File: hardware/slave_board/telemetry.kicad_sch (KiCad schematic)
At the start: 0 parts

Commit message: feat(hw): complete Telemetry schematic, ADS1115 integration and voltage divider
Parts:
- added U2: ADS1115IDGS, Package_SO:TSSOP-10_3x3mm_P0.5mm, symbol Analog_ADC:ADS1115IDGS
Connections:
- new net +3.3V: U2.8 (VDD)
- new net ADC_ALERT: U2.2 (ALERT/RDY)
- new net GND: U2.1 (ADDR), U2.3 (GND)
- new net I2C_SCL: U2.10 (SCL)
- new net I2C_SDA: U2.9 (SDA)

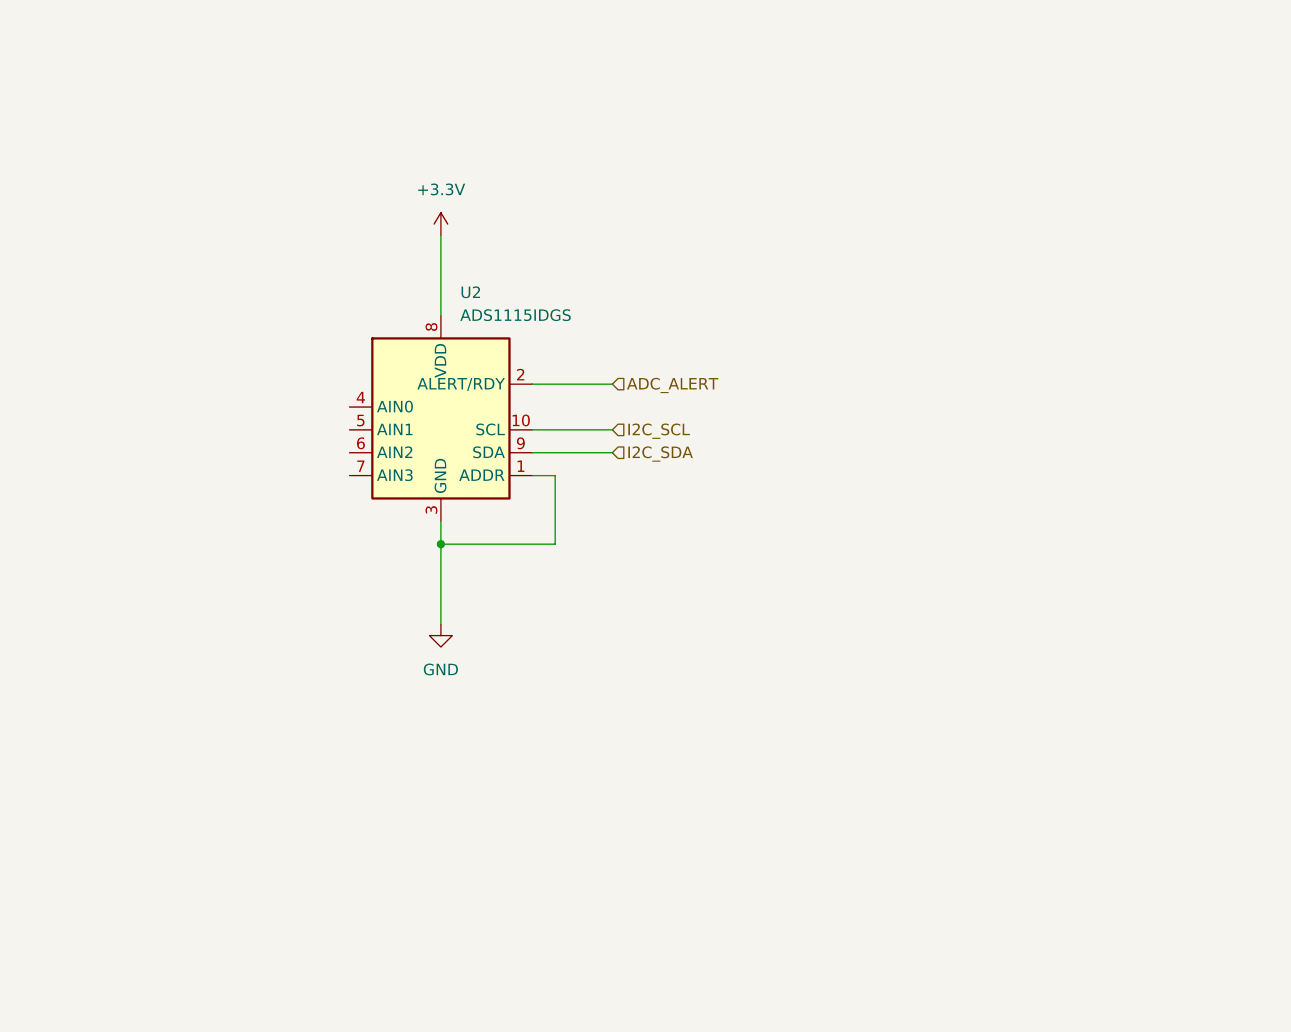
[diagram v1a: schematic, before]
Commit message: feat(hw): add Master-board RJ45 protection circuit with PTC and BAT54S clamps
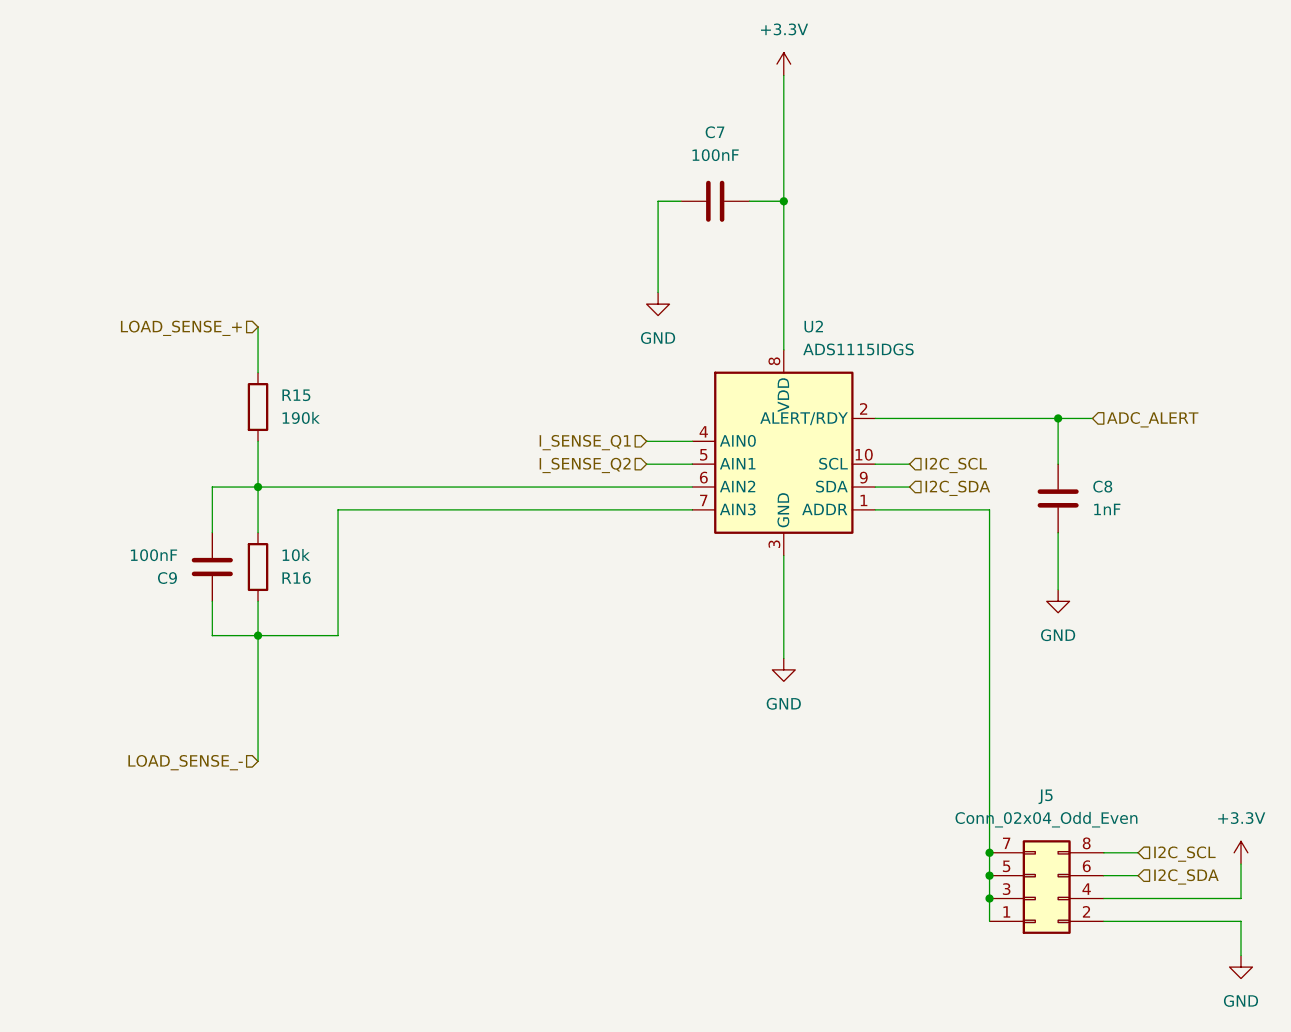
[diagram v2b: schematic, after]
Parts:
- added C7: 100nF, symbol Device:C
- added C8: 1nF, symbol Device:C
- added C9: 100nF, Capacitor_SMD:C_0805_2012Metric_Pad1.18x1.45mm_HandSolder, symbol Device:C
- added J5: Conn_02x04_Odd_Even, symbol Connector_Generic:Conn_02x04_Odd_Even
- added R15: 190k, Resistor_SMD:R_1206_3216Metric_Pad1.30x1.75mm_HandSolder, symbol Device:R
- added R16: 10k, Resistor_SMD:R_0805_2012Metric_Pad1.20x1.40mm_HandSolder, symbol Device:R
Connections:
- net +3.3V: now also C7.2, J5.4 (Pin_4)
- net ADC_ALERT: now also C8.1
- net GND: now also C7.1, C8.2, J5.2 (Pin_2); no longer U2.1 (ADDR)
- net I2C_SCL: now also J5.8 (Pin_8)
- net I2C_SDA: now also J5.6 (Pin_6)
- net I_SENSE_Q1: now reaches U2.4 (AIN0)
- net I_SENSE_Q2: now reaches U2.5 (AIN1)
- net at U2.6 (AIN2): now also C9.2, R15.2, R16.2
- net LOAD_SENSE_-: now reaches U2.7 (AIN3)
- net LOAD_SENSE_-: now also C9.1, R16.1
- new net: J5.1 (Pin_1), J5.3 (Pin_3), J5.5 (Pin_5), J5.7 (Pin_7), U2.1 (ADDR)
- new net LOAD_SENSE_+: R15.1
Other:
- moved on the sheet: U2

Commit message: hw(slave): fix footprints, enforce HandSolder, defer connector selection
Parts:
- C7, C8: footprint (none) -> Capacitor_SMD:C_0805_2012Metric_Pad1.18x1.45mm_HandSolder
- J5: footprint (none) -> Connector_PinHeader_2.54mm:PinHeader_2x04_P2.54mm_Vertical
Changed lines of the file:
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@@
 			)
 		)
-		(property "Footprint" ""
+		(property "Footprint" "Capacitor_SMD:C_0805_2012Metric_Pad1.18x1.45mm_HandSolder"
 			(at 182.5752 99.06 0)
 			(hide yes)
@@
 			)
 		)
-		(property "Description" "Unpolarized capacitor"
+		(property "Description" "Ceramic Capacitor SMD 1nF, 50V, C0G/NP0, 0805"
 			(at 181.61 95.25 0)
 			(hide yes)
@@
 			)
 		)
-		(property "Footprint" ""
+		(property "Footprint" "Capacitor_SMD:C_0805_2012Metric_Pad1.18x1.45mm_HandSolder"
 			(at 147.32 61.2648 0)
 			(hide yes)
@@
 			)
 		)
-		(property "Description" "Unpolarized capacitor"
+		(property "Description" "Ceramic Capacitor SMD 100nF, 50V, X7R, 0805"
 			(at 143.51 62.23 0)
 			(hide yes)
@@
 			)
 		)
-		(property "Footprint" ""
+		(property "Footprint" "Connector_PinHeader_2.54mm:PinHeader_2x04_P2.54mm_Vertical"
 			(at 179.07 139.7 0)
 			(hide yes)

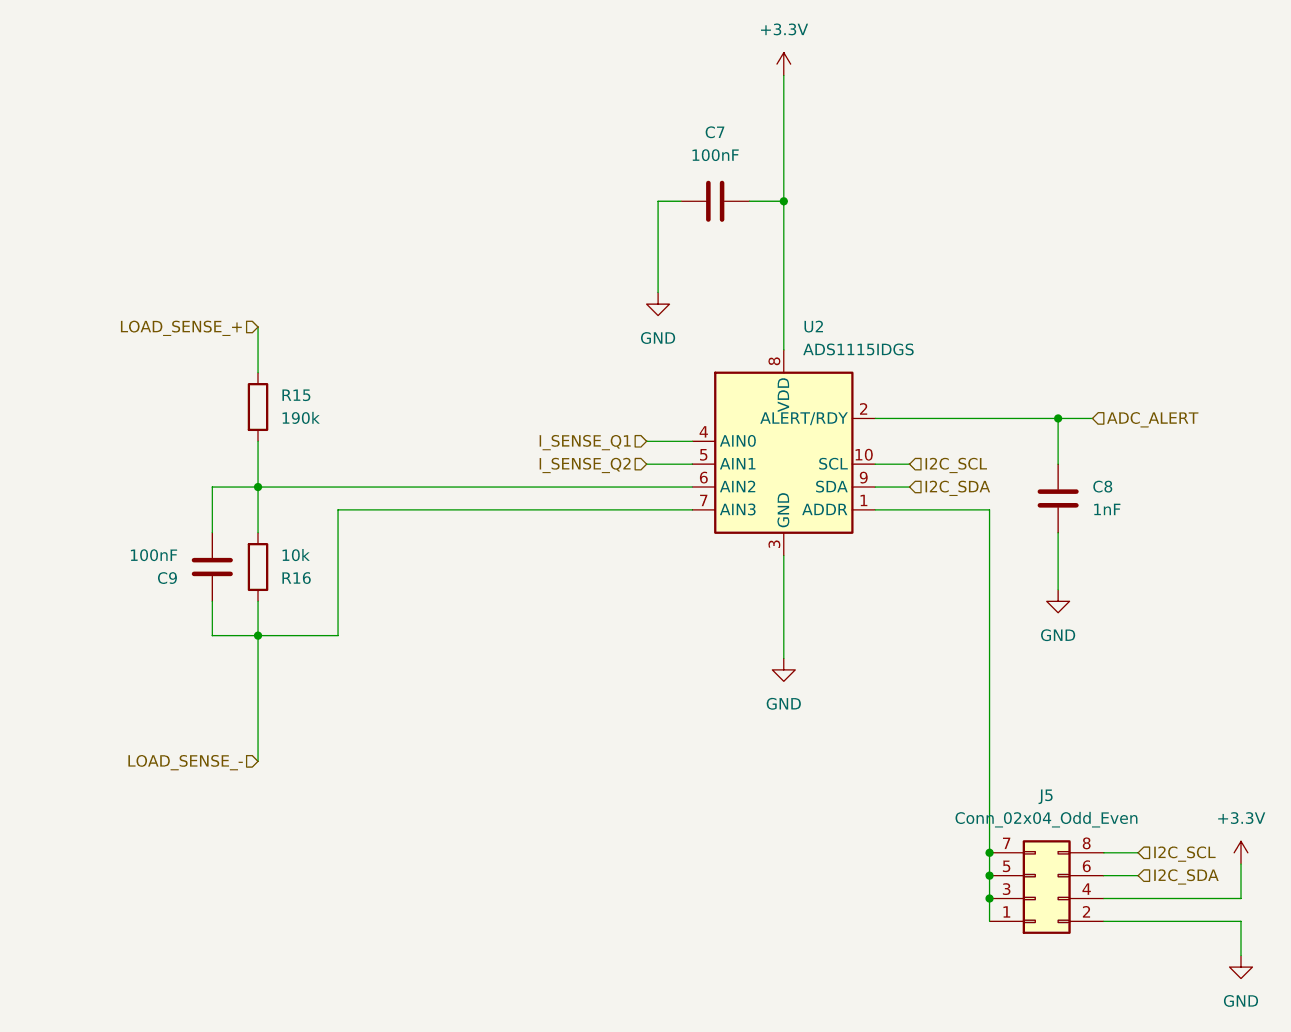
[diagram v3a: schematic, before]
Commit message: Implement cooling sheet, fan control, and update power connectors
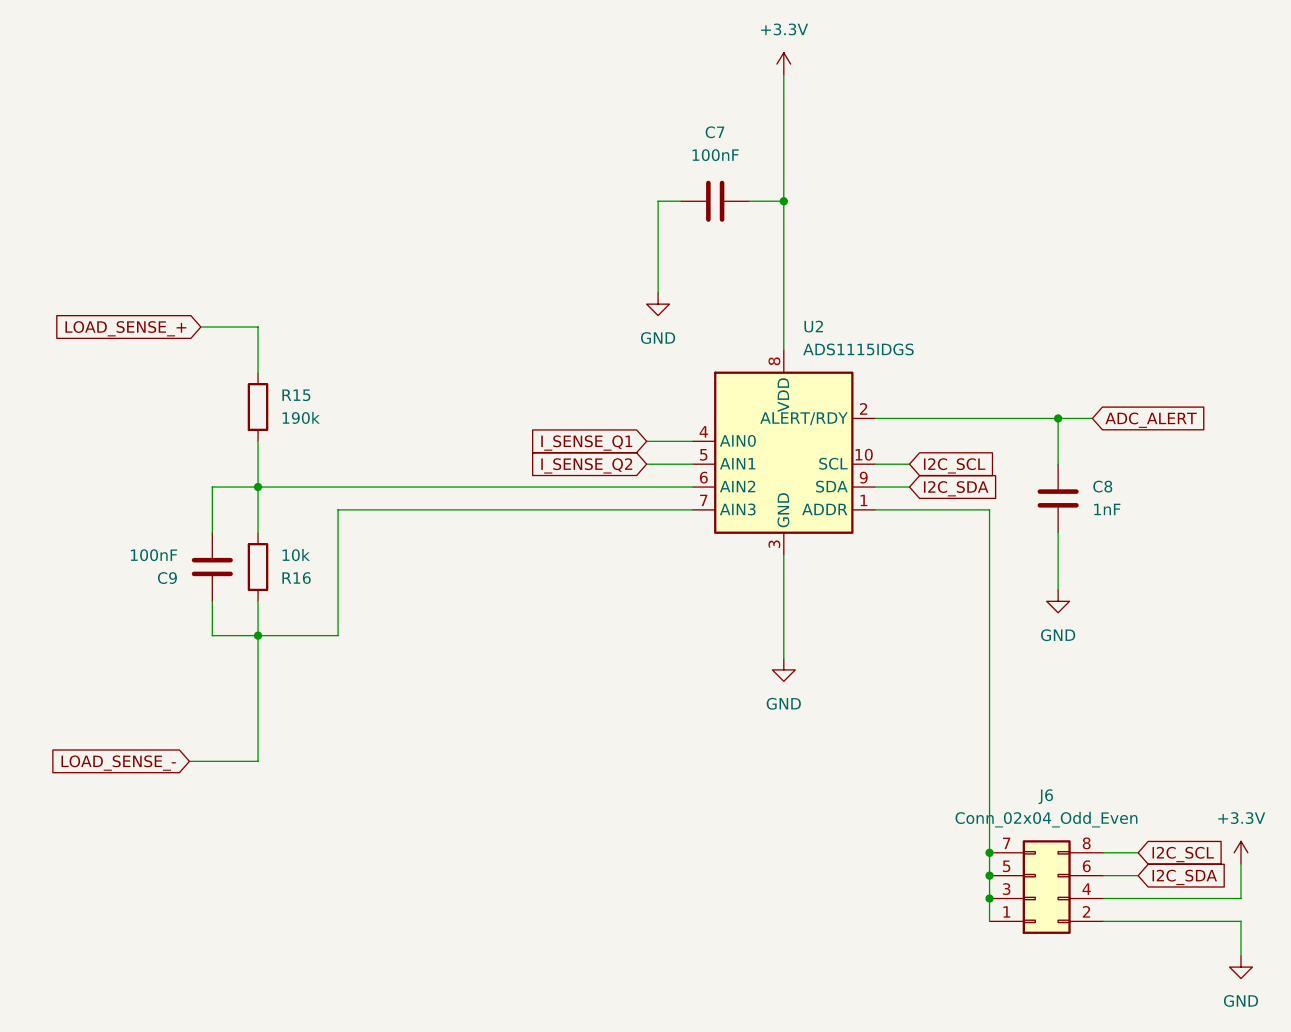
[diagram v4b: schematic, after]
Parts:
- renumbered J5 to J6
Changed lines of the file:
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@@
+	(wire
+		(pts
+			(xy 86.36 76.2) (xy 92.71 76.2)
+		)
+		(stroke
+			(width 0)
+			(type default)
+		)
+	)
 	(wire
 		(pts
@@
 	(wire
 		(pts
+			(xy 85.09 124.46) (xy 92.71 124.46)
+		)
+		(stroke
+			(width 0)
+			(type default)
+		)
+	)
+	(wire
+		(pts
 			(xy 87.63 99.06) (xy 87.63 93.98)
 		)
@@
 		)
 	)
-	(hierarchical_label "LOAD_SENSE_+"
+	(global_label "I2C_SDA"
 		(shape input)
-		(at 92.71 76.2 180)
+		(at 165.1 93.98 0)
+		(fields_autoplaced yes)
 		(effects
 			(font
 				(size 1.27 1.27)
 			)
-			(justify right)
-		)
-	)
-	(hierarchical_label "I2C_SDA"
+			(justify left)
+		)
+		(property "Intersheetrefs" "${INTERSHEET_REFS}"
+			(at 175.7052 93.98 0)
+			(hide yes)
+			(show_name no)
+			(do_not_autoplace no)
+			(effects
+				(font
+					(size 1.27 1.27)
+				)
+				(justify left)
+			)
+		)
+	)
+	(global_label "I_SENSE_Q2"
 		(shape input)
-		(at 165.1 93.98 0)
+		(at 135.89 91.44 180)
+		(fields_autoplaced yes)
 		(effects
 			(font
 				(size 1.27 1.27)
 			)
-			(justify left)
-		)
-	)
-	(hierarchical_label "ADC_ALERT"
+			(justify right)
+		)
+		(property "Intersheetrefs" "${INTERSHEET_REFS}"
+			(at 121.7773 91.44 0)
+			(hide yes)
+			(show_name no)
+			(do_not_autoplace no)
+			(effects
+				(font
+					(size 1.27 1.27)
+				)
+				(justify right)
+			)
+		)
+	)
+	(global_label "LOAD_SENSE_-"
 		(shape input)
-		(at 185.42 86.36 0)
+		(at 85.09 124.46 180)
+		(fields_autoplaced yes)
 		(effects
 			(font
 				(size 1.27 1.27)
 			)
-			(justify left)
-		)
-	)
-	(hierarchical_label "I_SENSE_Q2"
+			(justify right)
+		)
+		(property "Intersheetrefs" "${INTERSHEET_REFS}"
+			(at 67.8325 124.46 0)
+			(hide yes)
+			(show_name no)
+			(do_not_autoplace no)
+			(effects
+				(font
+					(size 1.27 1.27)
+				)
+				(justify right)
+			)
+		)
+	)
+	(global_label "I2C_SCL"
 		(shape input)
-		(at 135.89 91.44 180)
+		(at 190.5 134.62 0)
+		(fields_autoplaced yes)
 		(effects
 			(font
 				(size 1.27 1.27)
 			)
-			(justify right)
-		)
-	)
-	(hierarchical_label "I_SENSE_Q1"
+			(justify left)
+		)
+		(property "Intersheetrefs" "${INTERSHEET_REFS}"
+			(at 201.0447 134.62 0)
+			(hide yes)
+			(show_name no)
+			(do_not_autoplace no)
+			(effects
+				(font
+					(size 1.27 1.27)
+				)
+				(justify left)
+			)
+		)
+	)
+	(global_label "I_SENSE_Q1"
 		(shape input)
 		(at 135.89 88.9 180)
+		(fields_autoplaced yes)
 		(effects
 			(font
@@
 			(justify right)
 		)
-	)
-	(hierarchical_label "I2C_SCL"
+		(property "Intersheetrefs" "${INTERSHEET_REFS}"
+			(at 121.7773 88.9 0)
+			(hide yes)
+			(show_name no)
+			(do_not_autoplace no)
+			(effects
+				(font
+					(size 1.27 1.27)
+				)
+				(justify right)
+			)
+		)
+	)
+	(global_label "ADC_ALERT"
 		(shape input)
-		(at 165.1 91.44 0)
+		(at 185.42 86.36 0)
+		(fields_autoplaced yes)
 		(effects
 			(font
@@
 			(justify left)
 		)
-	)
-	(hierarchical_label "LOAD_SENSE_-"
+		(property "Intersheetrefs" "${INTERSHEET_REFS}"
+			(at 198.5047 86.36 0)
+			(hide yes)
+			(show_name no)
+			(do_not_autoplace no)
+			(effects
+				(font
+					(size 1.27 1.27)
+				)
+				(justify left)
+			)
+		)
+	)
+	(global_label "I2C_SCL"
 		(shape input)
-		(at 92.71 124.46 180)
+		(at 165.1 91.44 0)
+		(fields_autoplaced yes)
 		(effects
 			(font
 				(size 1.27 1.27)
 			)
-			(justify right)
-		)
-	)
-	(hierarchical_label "I2C_SDA"
+			(justify left)
+		)
+		(property "Intersheetrefs" "${INTERSHEET_REFS}"
+			(at 175.6447 91.44 0)
+			(hide yes)
+			(show_name no)
+			(do_not_autoplace no)
+			(effects
+				(font
+					(size 1.27 1.27)
+				)
+				(justify left)
+			)
+		)
+	)
+	(global_label "I2C_SDA"
 		(shape input)
 		(at 190.5 137.16 0)
+		(fields_autoplaced yes)
 		(effects
 			(font
@@
 			(justify left)
 		)
-	)
-	(hierarchical_label "I2C_SCL"
+		(property "Intersheetrefs" "${INTERSHEET_REFS}"
+			(at 201.1052 137.16 0)
+			(hide yes)
+			(show_name no)
+			(do_not_autoplace no)
+			(effects
+				(font
+					(size 1.27 1.27)
+				)
+				(justify left)
+			)
+		)
+	)
+	(global_label "LOAD_SENSE_+"
 		(shape input)
-		(at 190.5 134.62 0)
+		(at 86.36 76.2 180)
+		(fields_autoplaced yes)
 		(effects
 			(font
 				(size 1.27 1.27)
 			)
-			(justify left)
+			(justify right)
+		)
+		(property "Intersheetrefs" "${INTERSHEET_REFS}"
+			(at 69.1025 76.2 0)
+			(hide yes)
+			(show_name no)
+			(do_not_autoplace no)
+			(effects
+				(font
+					(size 1.27 1.27)
+				)
+				(justify right)
+			)
 		)
 	)
@@
 		(dnp no)
 		(fields_autoplaced yes)
-		(property "Reference" "J5"
+		(property "Reference" "J6"
 			(at 180.34 128.27 0)
 			(show_name no)
@@
 			(project "slave_board"
 				(path "/2c4fc43b-02b1-4ef7-8914-a684f462c899/66d25d5f-b49c-4f1e-a839-fa51026b9740"
-					(reference "J5")
+					(reference "J6")
 					(unit 1)
 				)
